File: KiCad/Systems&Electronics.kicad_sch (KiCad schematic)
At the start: 34 parts, among them U3 MAX485E, U4 MAX485E

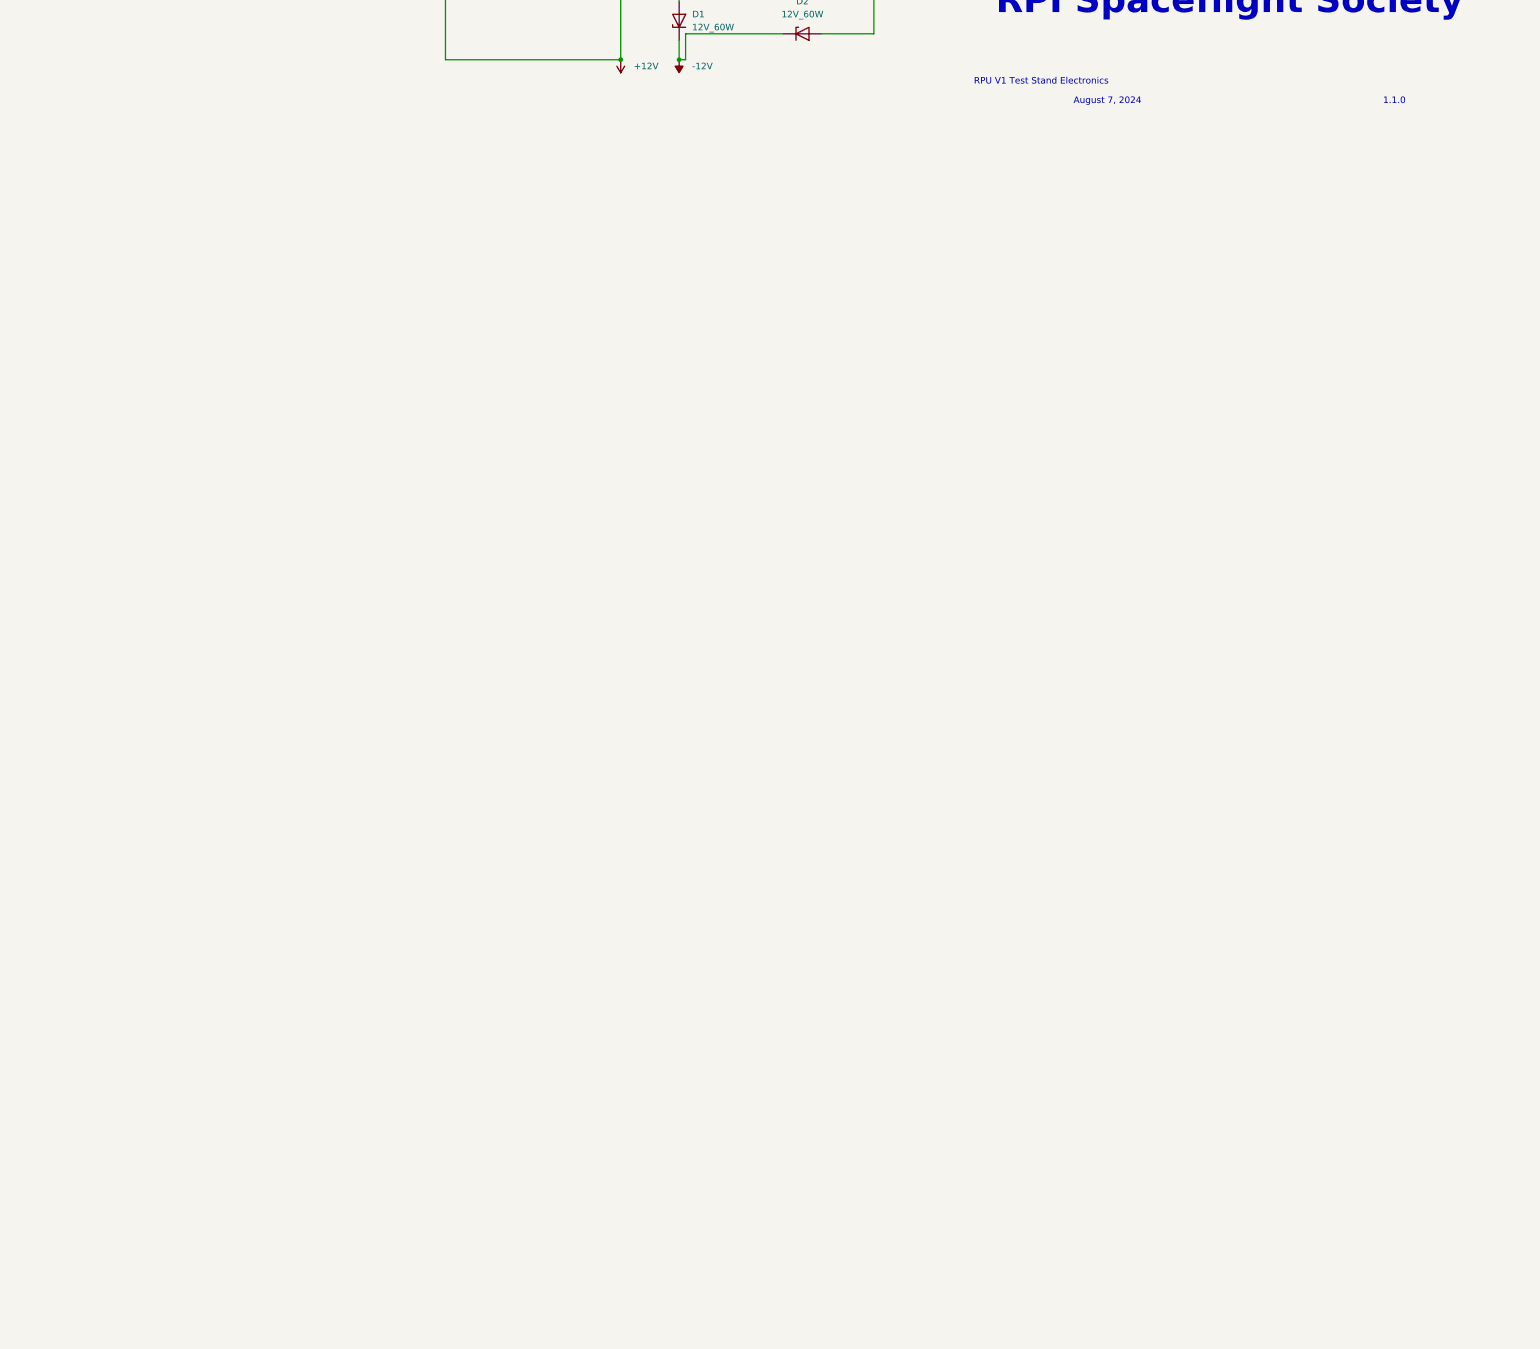
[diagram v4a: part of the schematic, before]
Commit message: Add the Control Room Side of the Signal Decode
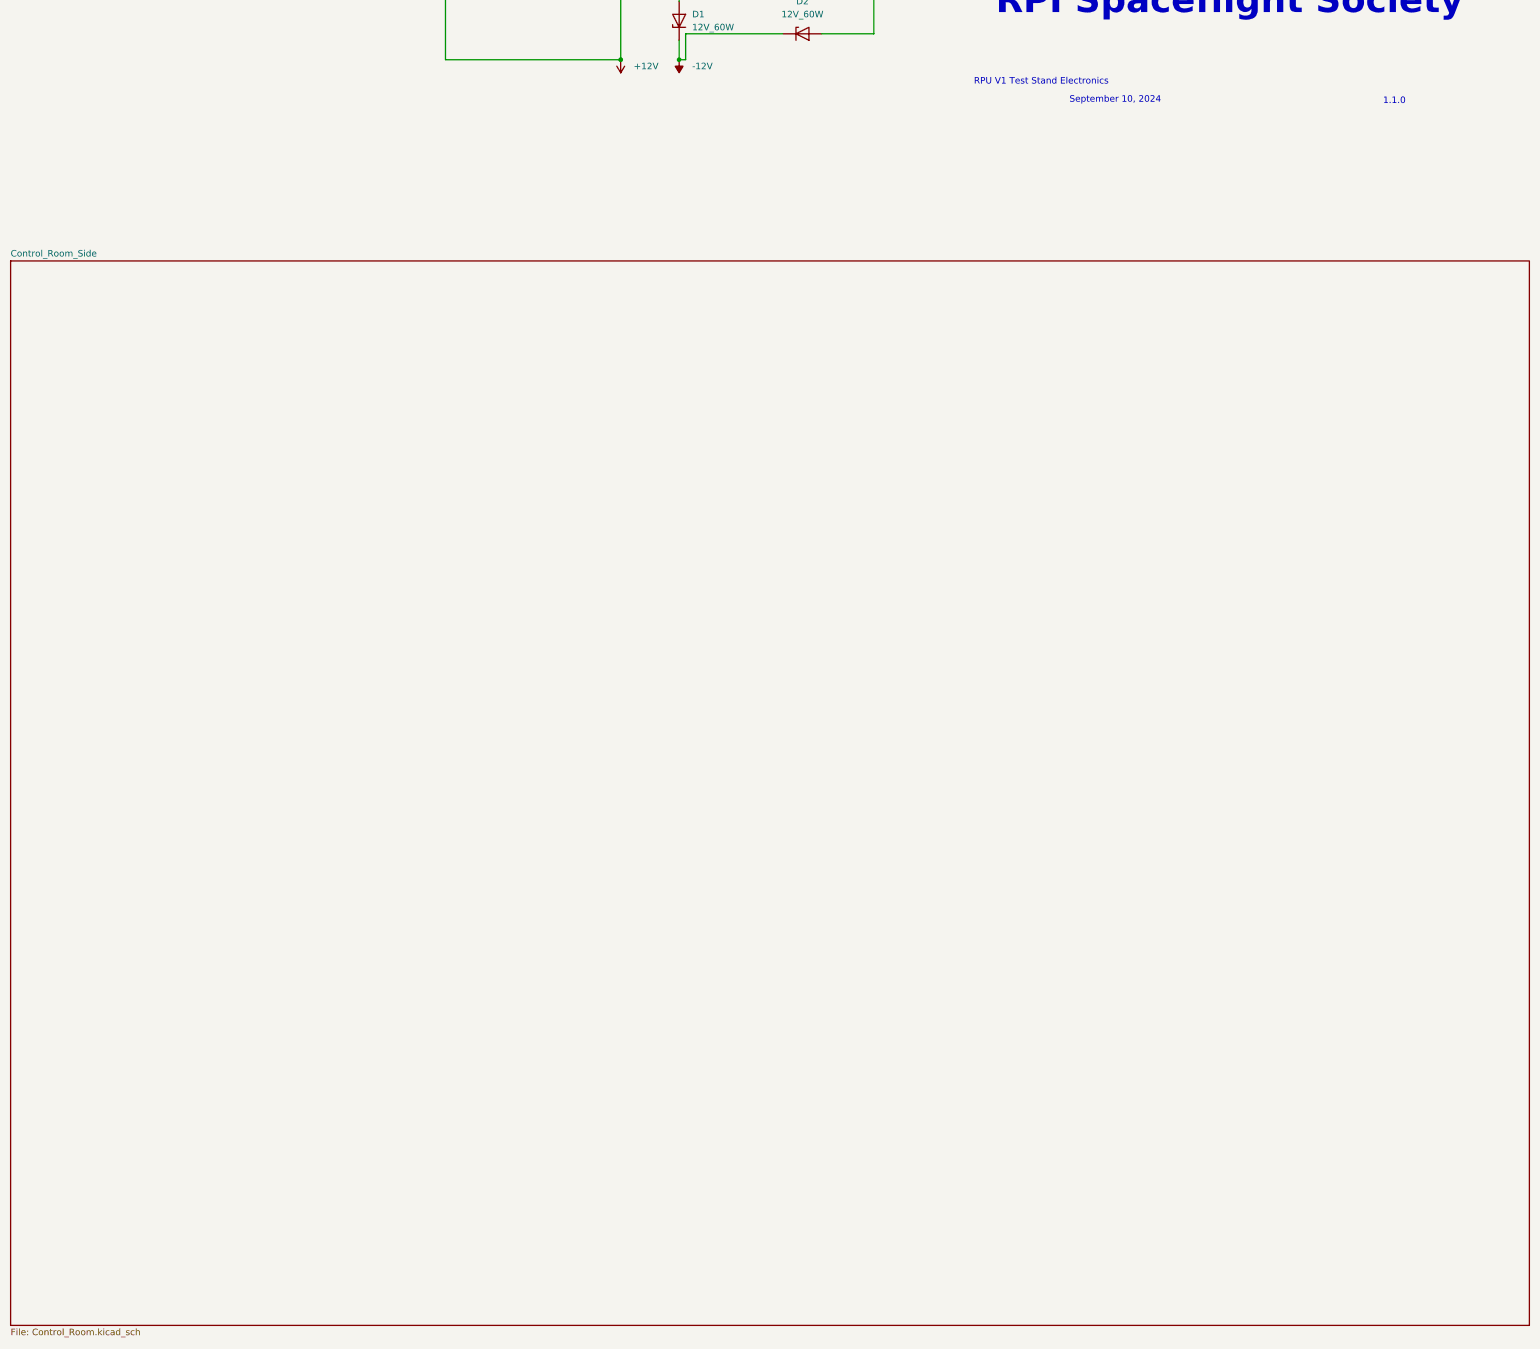
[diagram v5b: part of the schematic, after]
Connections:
- net at Solenoid1. (-): now also D2.2 (A), D3.1 (K), Solenoid2. (-), Solenoid3. (-); no longer 5V Relay1. (NO)
- net at Pressure_Transducer1. (VCC), Pressure_Transducer2. (VCC), Pressure_Transducer3. (VCC)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: now also A1.GND1 (GND); no longer A1.5V3 (5V)
- new net: 5V Relay1. (NO), 5V Relay2. (NO), 5V Relay3. (NO), 5V Relay4. (NO), A1.5V4 (5V)
- new net: 5V Relay1. (NO), 5V Relay2. (NO), 5V Relay3. (NO), 5V Relay4. (NO), A1.GND3 (GND)
- new net: 5V Relay1. (NO), Solenoid1. (-)
- new net: A1.5V3 (5V), Pressure_Transducer1. (VCC), Pressure_Transducer2. (VCC), Pressure_Transducer3. (VCC), Pressure_Transducer4. (VCC), Pressure_Transducer5. (VCC), Pressure_Transducer6. (VCC)
- new net: HX711_Board1. (VCC), Load_Cell1. (VCC) (x3)
- new net: 5V Relay3. (NO), Solenoid3. (-)
- new net: MAX6675_1. (VCC), Thermocouple1. (-)
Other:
- added sheet Control_Room_Side (Control_Room.kicad_sch)
- note added: "September 10, 2024"
- note removed: "August 7, 2024"
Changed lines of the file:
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@@
 		)
 	)
-	(text "August 7, 2024"
-		(exclude_from_sim no)
-		(at 214.63 193.548 0)
+	(text "September 10, 2024"
+		(exclude_from_sim no)
+		(at 216.154 193.294 0)
 		(effects
 			(font
@@
 				)
 			)
+		)
+	)
+	(sheet
+		(at 0 224.79)
+		(size 297.18 208.28)
+		(fields_autoplaced yes)
+		(stroke
+			(width 0.1524)
+			(type solid)
+			(color 255 255 255 1)
+		)
+		(fill
+			(color 0 0 0 0.0000)
+		)
+		(property "Sheetname" "Control_Room_Side"
+			(at 0 224.0784 0)
+			(effects
+				(font
+					(size 1.27 1.27)
+				)
+				(justify left bottom)
+			)
+		)
+		(property "Sheetfile" "Control_Room.kicad_sch"
+			(at 0 433.6546 0)
+			(effects
+				(font
+					(size 1.27 1.27)
+				)
+				(justify left top)
+			)
+		)
+		(instances
+			(project "Systems&Electronics"
+				(path "/4e05caf8-77e4-4a22-9a05-51fcca8e50ff"
+					(page "2")
+				)
+			)

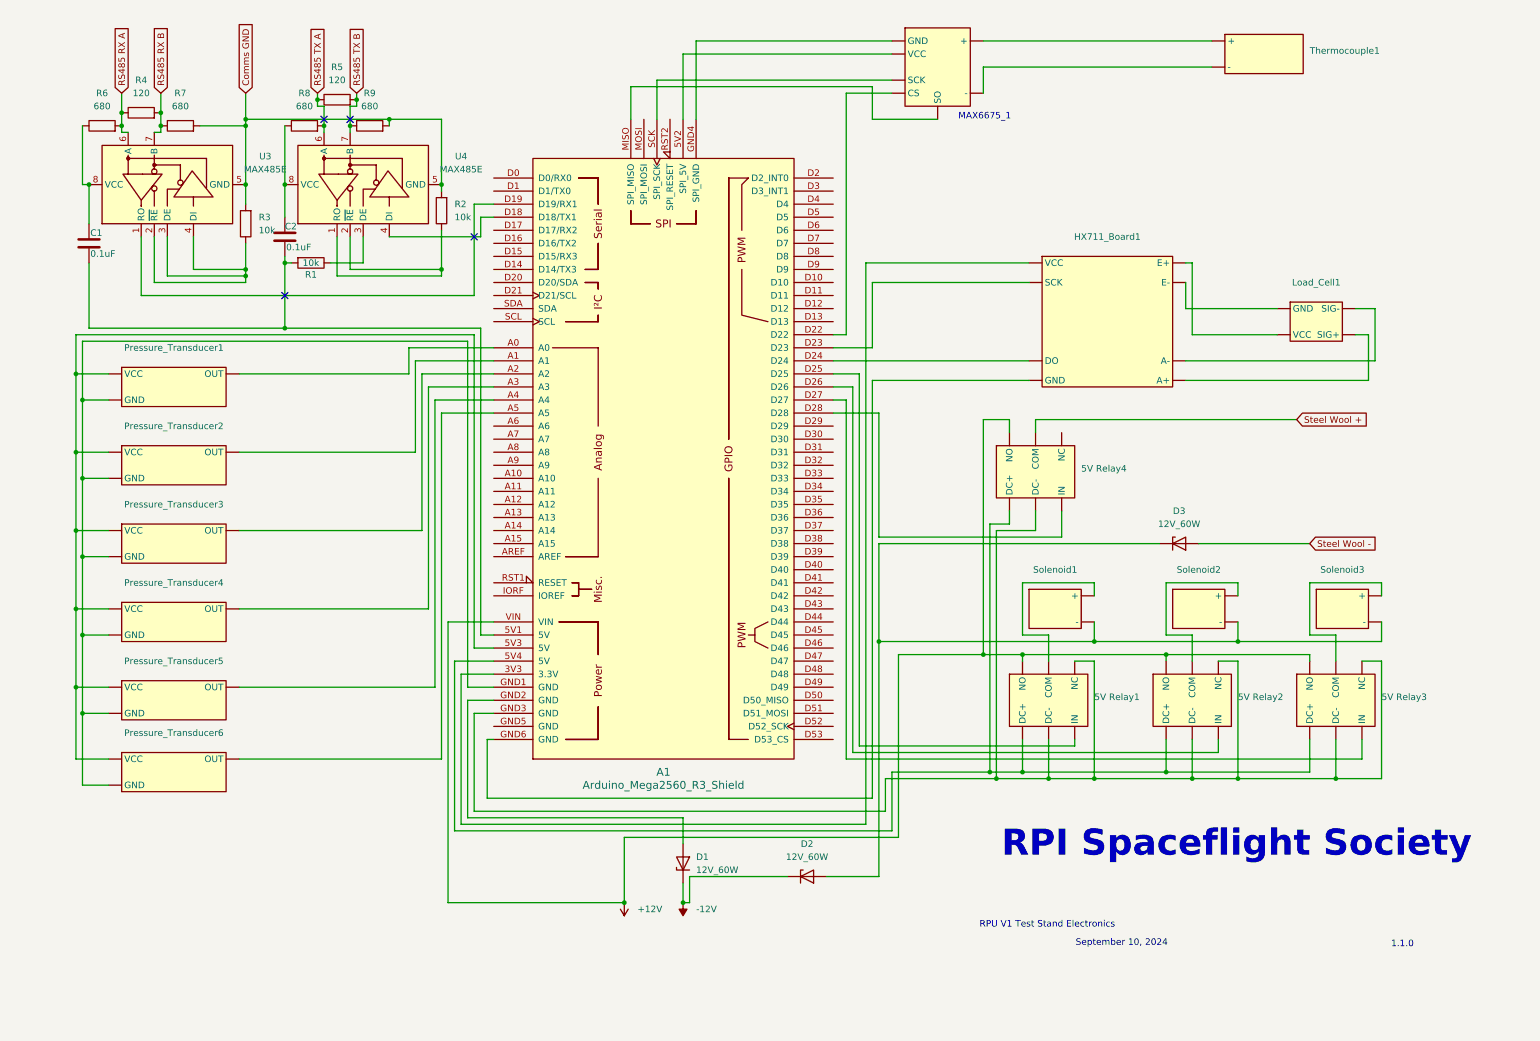
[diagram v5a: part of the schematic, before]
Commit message: Thermocouples
I added thermocouples to the systems schematic.
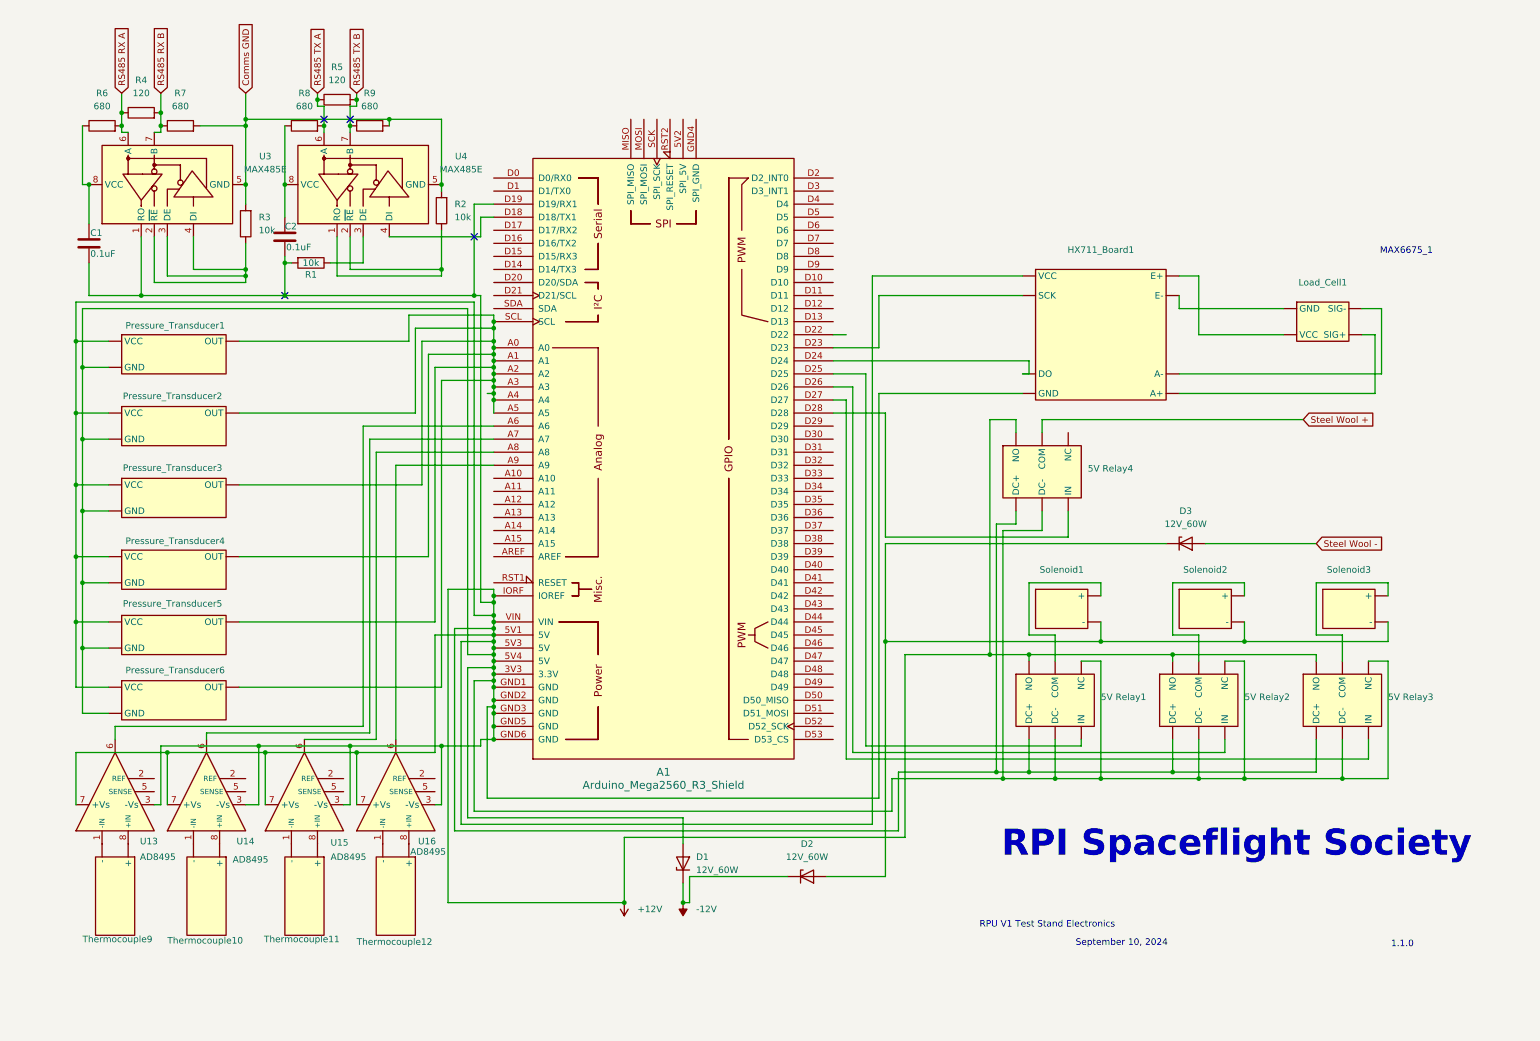
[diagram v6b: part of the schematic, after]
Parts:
- removed MAX6675_1: ~, symbol MAX6675:MAX6675
- removed Thermocouple1: ~, symbol Sensors:Thermocouple
- added Thermocouple10, Thermocouple11, Thermocouple12, Thermocouple9: ~, symbol Sensors:Thermocouple
- added U13, U14, U15, U16: AD8495, Package_SO:MSOP-8_3x3mm_P0.65mm, symbol Sensor_Temperature:AD8495
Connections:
- net +12V: now also A1.3V3 (3.3V), A1.5V1 (5V), A1.5V3 (5V), A1.5V4 (5V), A1.D19 (D19/RX1), A1.GND1 (GND), A1.GND2 (GND), A1.GND3 (GND), A1.GND5 (GND), A1.GND6 (GND), A1.IORF (IOREF), C1.2, C2.1, D1.2 (A), HX711_Board1. (VCC), Pressure_Transducer1. (VCC), Pressure_Transducer2. (VCC), Pressure_Transducer3. (VCC), Pressure_Transducer4. (VCC), Pressure_Transducer5. (VCC), Pressure_Transducer6. (VCC), R1.2, U3.1 (RO), U13.3 (-Vs), U13.7 (+Vs), U14.3 (-Vs), U14.7 (+Vs), U15.3 (-Vs), U15.7 (+Vs), U16.3 (-Vs), U16.7 (+Vs)
- net at Solenoid1. (-): now also D2.2 (A), D3.1 (K), Solenoid2. (-), Solenoid3. (-); no longer 5V Relay1. (NO)
- net at A1.A0, Pressure_Transducer1. (VCC): now also A1.A1, A1.A2, A1.A3, A1.A4, A1.A5, A1.SCL, Pressure_Transducer2. (VCC), Pressure_Transducer3. (VCC), Pressure_Transducer4. (VCC), Pressure_Transducer5. (VCC), Pressure_Transducer6. (VCC)
- net at A1.A6: now also U13.6
- net at A1.A7: now also U14.6
- net at A1.A8: now also U15.6
- net at A1.A9: now also U16.6
- new net: Thermocouple9. (-), U13.1 (-IN)
- new net: Thermocouple9. (-), U13.8 (+IN)
- new net: 5V Relay1. (NO), Solenoid1. (-)
- new net: HX711_Board1. (VCC), Load_Cell1. (VCC) (x3)
- new net: 5V Relay3. (NO), Solenoid3. (-)
- new net: Thermocouple12. (-), U16.1 (-IN)
- new net: Thermocouple12. (-), U16.8 (+IN)
- new net: Thermocouple11. (-), U15.1 (-IN)
- new net: Thermocouple11. (-), U15.8 (+IN)
- new net: Thermocouple10. (-), U14.1 (-IN)
- new net: Thermocouple10. (-), U14.8 (+IN)
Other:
- moved on the sheet: 5V Relay1, 5V Relay2, 5V Relay3, 5V Relay4, D3, HX711_Board1, Load_Cell1, Pressure_Transducer1, Pressure_Transducer2, Pressure_Transducer3, Pressure_Transducer4, Pressure_Transducer5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
